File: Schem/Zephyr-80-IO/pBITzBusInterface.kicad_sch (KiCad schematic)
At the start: 1 part, among them J1 pBITzBus

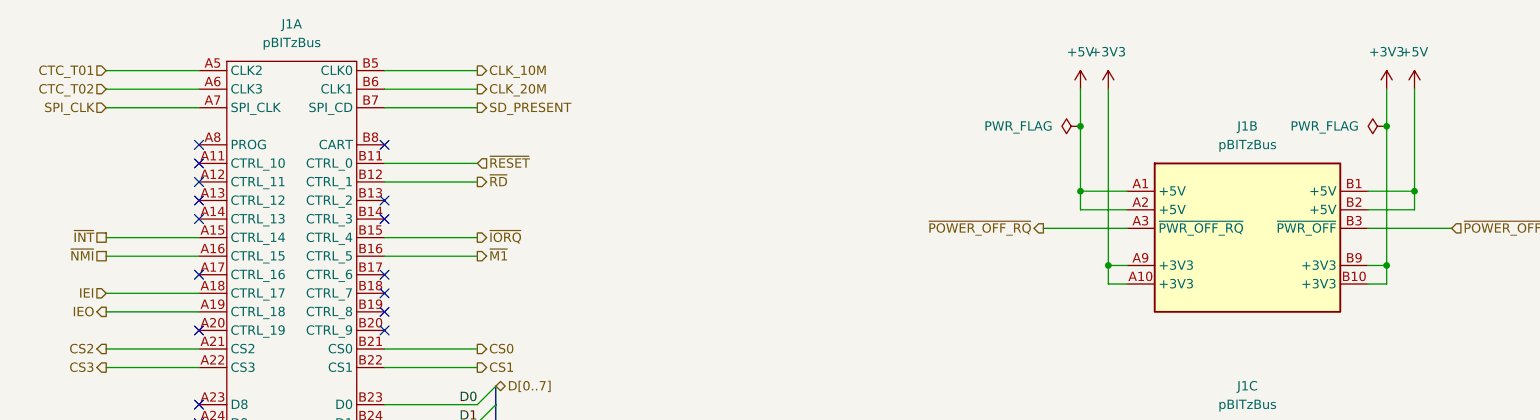
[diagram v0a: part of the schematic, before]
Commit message: Completed the IO Controller schematic and PCB layout for the Zephyr-80 project. This includes the design of the Baud Clock, CPU Address Decoding, Console Port, Device Select Decode, GPIO User Serial, and the main IO Controller schematics. Additionally, the PCB layout for the Zephyr-80 IO board has been created, along with the necessary library files and documentation for the control signal mapping.
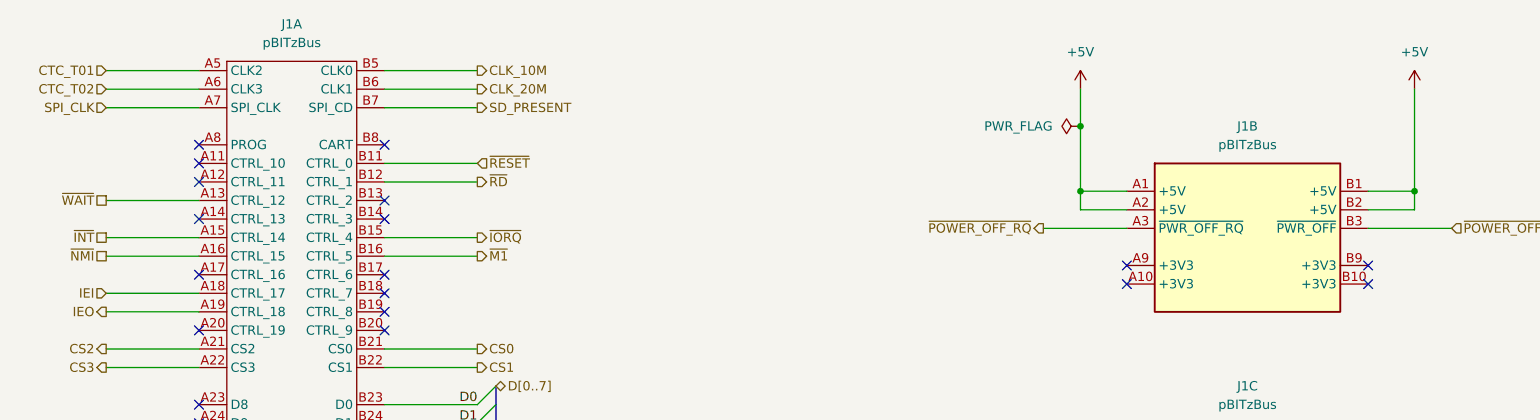
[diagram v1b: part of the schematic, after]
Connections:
- net ~{WAIT}: now reaches J1.A13 (CTRL_12)
- removed net +3V3: J1.A10 (+3V3), J1.A9 (+3V3), J1.B10 (+3V3), J1.B9 (+3V3)
- no-connect marks 44 -> 47
